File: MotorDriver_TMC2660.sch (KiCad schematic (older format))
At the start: 16 parts, among them U4 TMC2660

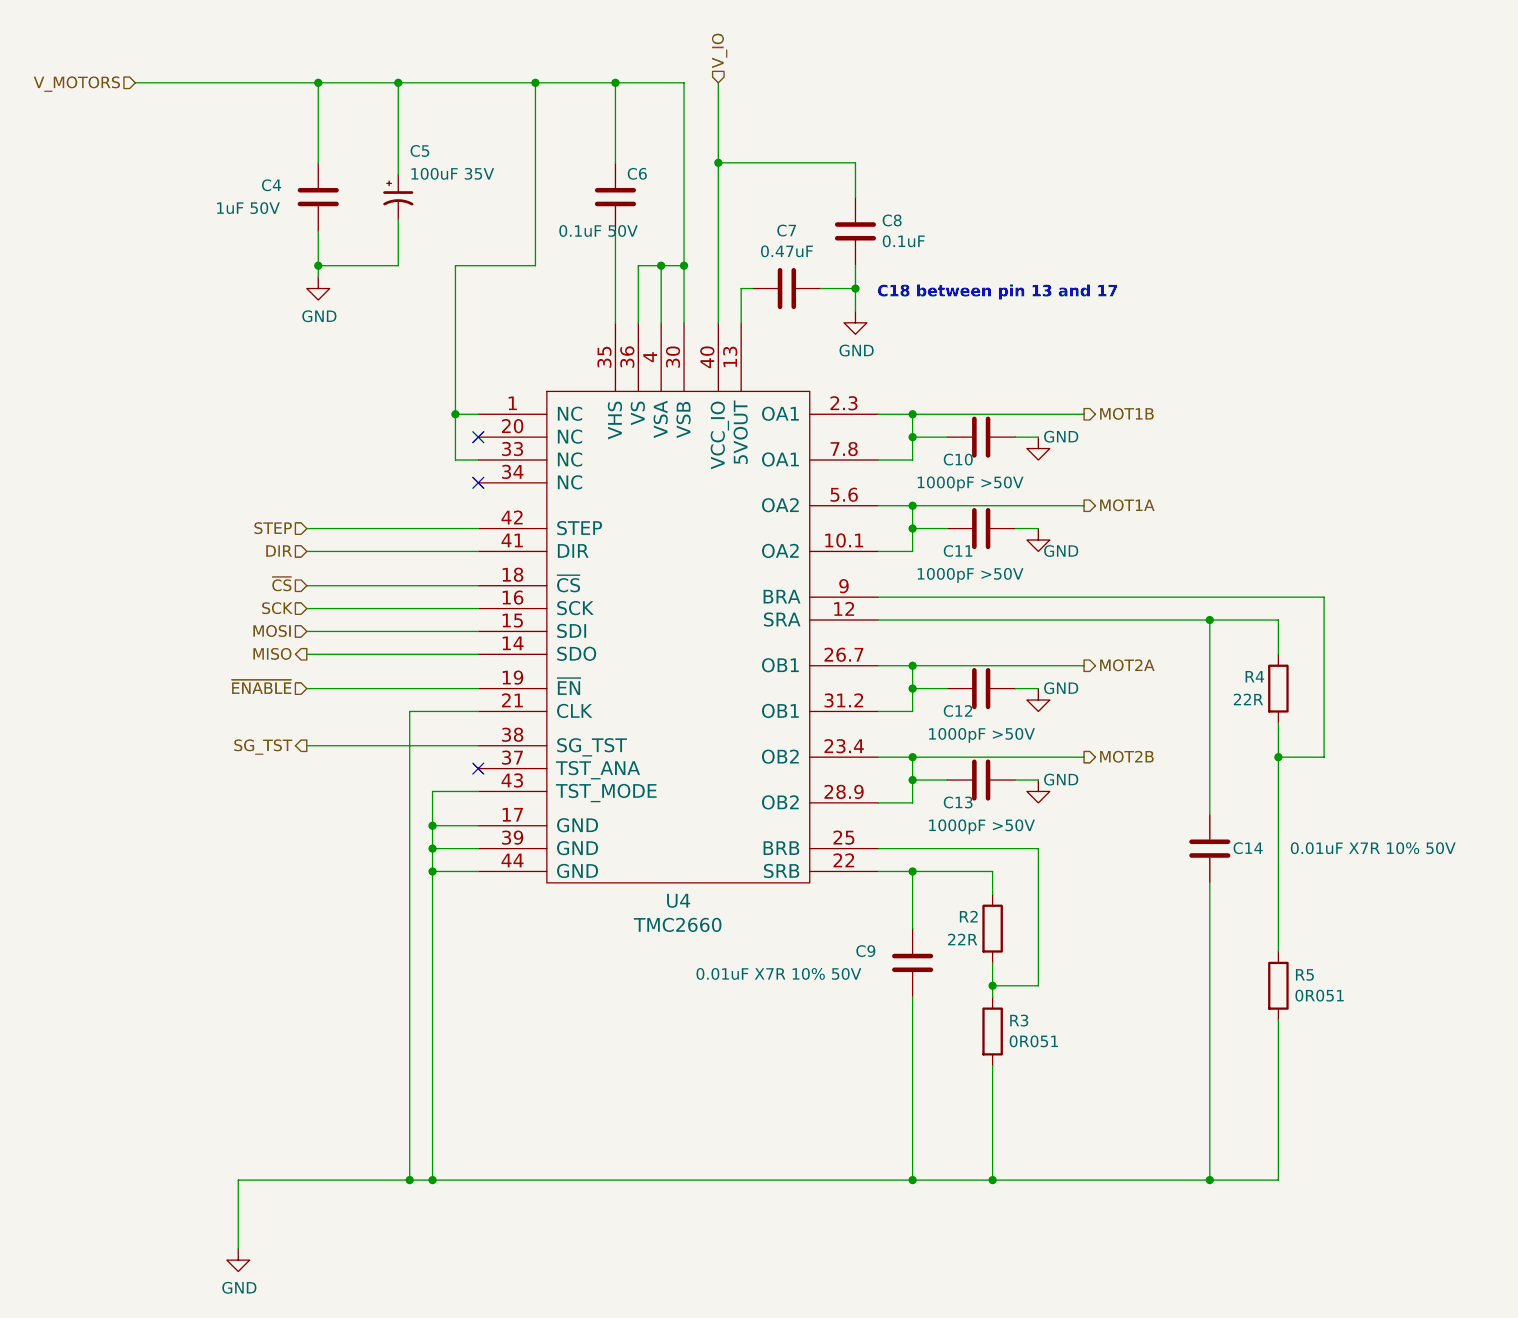
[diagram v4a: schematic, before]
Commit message: Assigned footprints for all components. Inductors are approximate size. MOSFETs dont agree with the footprints. Saved pcb netlist report as report.txt.
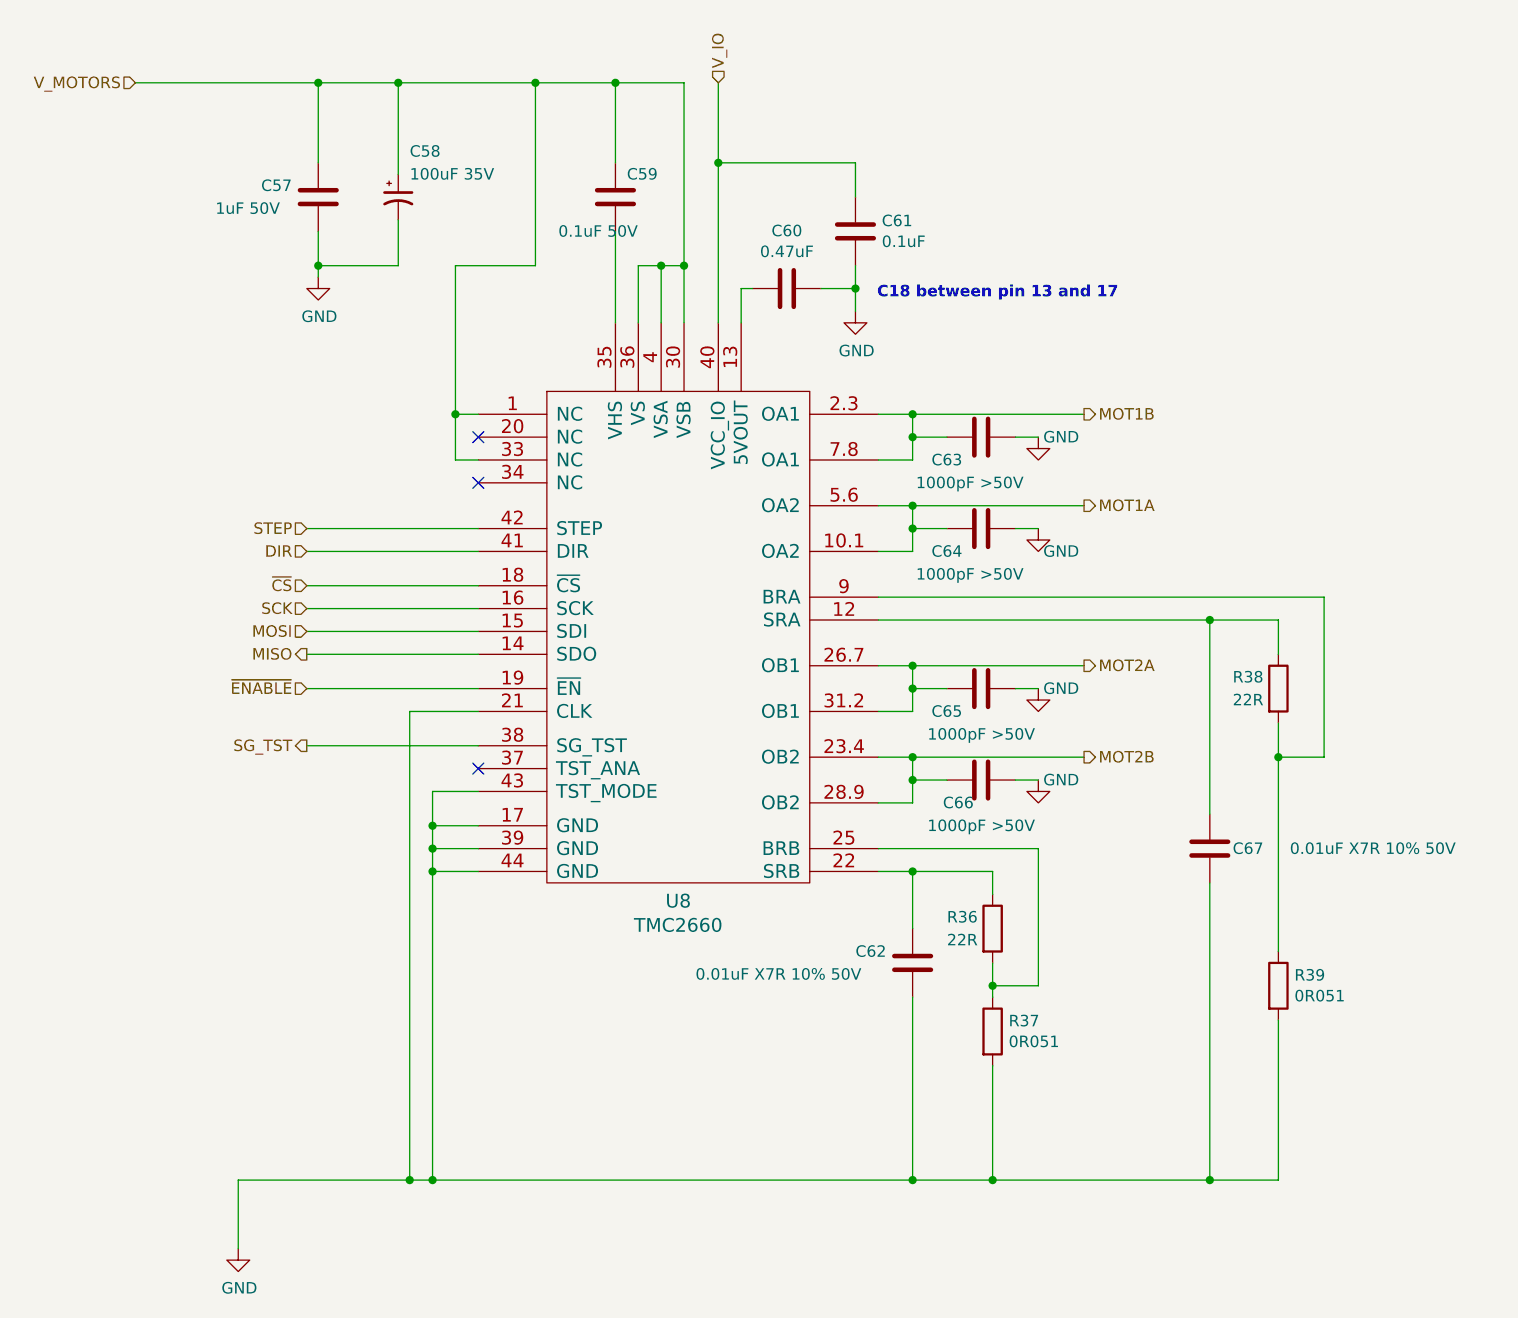
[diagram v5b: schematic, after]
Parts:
- C10, C11, C12, C13, C14, C4, C6, C7, C8, C9: footprint (none) -> Capacitor_SMD:C_0603_1608Metric
- C5: footprint (none) -> Capacitor_SMD:CP_Elec_6.3x7.7
- R2, R4: footprint (none) -> Resistor_SMD:R_0603_1608Metric
- R3, R5: footprint (none) -> Resistor_SMD:R_1206_3216Metric
- U4: footprint (none) -> PrntrBoardV1:TMC2660
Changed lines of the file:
@@
 $Descr A4 11693 8268
 encoding utf-8
-Sheet 9 35
+Sheet 26 35
 Title ""
 Date ""
@@
 AR Path="/5AC337B6/5ACE1C6D/5ACC0B66/5AC338BF" Ref="U7"  Part="1"
 AR Path="/5AC337B6/5AD9F95A/5AD4B0F5/5AC338BF" Ref="U8"  Part="1"
-F 0 "U4" H 4875 2520 60  0000 C CNN
+F 0 "U8" H 4875 2520 60  0000 C CNN
 F 1 "TMC2660" H 4875 2414 60  0000 C CNN
-F 2 "" H 4900 3600 60  0000 C CNN
+F 2 "PrntrBoardV1:TMC2660" H 4900 3600 60  0001 C CNN
 F 3 "" H 4900 3600 60  0000 C CNN
 	1    4900 3650
@@
 AR Path="/5AC337B6/5ACE1C6D/5ACC0B66/5AC33A94" Ref="C46"  Part="1"
 AR Path="/5AC337B6/5AD9F95A/5AD4B0F5/5AC33A94" Ref="C59"  Part="1"
-F 0 "C6" H 4650 1800 50  0000 L CNN
+F 0 "C59" H 4650 1800 50  0000 L CNN
 F 1 "0.1uF 50V" H 4350 1550 50  0000 L CNN
-F 2 "" H 4638 1550 50  0001 C CNN
+F 2 "Capacitor_SMD:C_0603_1608Metric" H 4638 1550 50  0001 C CNN
 F 3 "~" H 4600 1700 50  0001 C CNN
 	1    4600 1700
@@
 AR Path="/5AC337B6/5ACE1C6D/5ACC0B66/5AC33B3C" Ref="C44"  Part="1"
 AR Path="/5AC337B6/5AD9F95A/5AD4B0F5/5AC33B3C" Ref="C57"  Part="1"
-F 0 "C4" H 3050 1750 50  0000 L CNN
+F 0 "C57" H 3050 1750 50  0000 L CNN
 F 1 "1uF 50V" H 2850 1650 50  0000 L CNN
-F 2 "" H 3338 1550 50  0001 C CNN
+F 2 "Capacitor_SMD:C_0603_1608Metric" H 3338 1550 50  0001 C CNN
 F 3 "~" H 3300 1700 50  0001 C CNN
 	1    3300 1700
@@
 AR Path="/5AC337B6/5ACE1C6D/5ACC0B66/5AC33B85" Ref="C47"  Part="1"
 AR Path="/5AC337B6/5AD9F95A/5AD4B0F5/5AC33B85" Ref="C60"  Part="1"
-F 0 "C7" V 5098 2100 50  0000 C CNN
+F 0 "C60" V 5098 2100 50  0000 C CNN
 F 1 "0.47uF" V 5189 2100 50  0000 C CNN
-F 2 "" H 5388 1950 50  0001 C CNN
+F 2 "Capacitor_SMD:C_0603_1608Metric" H 5388 1950 50  0001 C CNN
 F 3 "~" H 5350 2100 50  0001 C CNN
 	1    5350 2100
@@
 AR Path="/5AC337B6/5ACE1C6D/5ACC0B66/5AC33C56" Ref="C48"  Part="1"
 AR Path="/5AC337B6/5AD9F95A/5AD4B0F5/5AC33C56" Ref="C61"  Part="1"
-F 0 "C8" H 5765 1896 50  0000 L CNN
+F 0 "C61" H 5765 1896 50  0000 L CNN
 F 1 "0.1uF" H 5765 1805 50  0000 L CNN
-F 2 "" H 5688 1700 50  0001 C CNN
+F 2 "Capacitor_SMD:C_0603_1608Metric" H 5688 1700 50  0001 C CNN
 F 3 "~" H 5650 1850 50  0001 C CNN
 	1    5650 1850
@@
 AR Path="/5AC337B6/5ACE1C6D/5ACC0B66/5AC33CA1" Ref="C50"  Part="1"
 AR Path="/5AC337B6/5AD9F95A/5AD4B0F5/5AC33CA1" Ref="C63"  Part="1"
-F 0 "C10" V 6300 2650 50  0000 C CNN
+F 0 "C63" V 6300 2600 50  0000 C CNN
 F 1 "1000pF >50V" V 6400 2700 50  0000 C CNN
-F 2 "" H 6238 2600 50  0001 C CNN
+F 2 "Capacitor_SMD:C_0603_1608Metric" H 6238 2600 50  0001 C CNN
 F 3 "~" H 6200 2750 50  0001 C CNN
 	1    6200 2750
@@
 AR Path="/5AC337B6/5ACE1C6D/5ACC0B66/5AC33D6E" Ref="C51"  Part="1"
 AR Path="/5AC337B6/5AD9F95A/5AD4B0F5/5AC33D6E" Ref="C64"  Part="1"
-F 0 "C11" V 6300 3050 50  0000 C CNN
+F 0 "C64" V 6300 3000 50  0000 C CNN
 F 1 "1000pF >50V" V 6400 3100 50  0000 C CNN
-F 2 "" H 6238 3000 50  0001 C CNN
+F 2 "Capacitor_SMD:C_0603_1608Metric" H 6238 3000 50  0001 C CNN
 F 3 "~" H 6200 3150 50  0001 C CNN
 	1    6200 3150
@@
 AR Path="/5AC337B6/5ACE1C6D/5ACC0B66/5AC33DC1" Ref="C52"  Part="1"
 AR Path="/5AC337B6/5AD9F95A/5AD4B0F5/5AC33DC1" Ref="C65"  Part="1"
-F 0 "C12" V 6300 3750 50  0000 C CNN
+F 0 "C65" V 6300 3700 50  0000 C CNN
 F 1 "1000pF >50V" V 6400 3850 50  0000 C CNN
-F 2 "" H 6238 3700 50  0001 C CNN
+F 2 "Capacitor_SMD:C_0603_1608Metric" H 6238 3700 50  0001 C CNN
 F 3 "~" H 6200 3850 50  0001 C CNN
 	1    6200 3850
@@
 AR Path="/5AC337B6/5ACE1C6D/5ACC0B66/5AC33E6E" Ref="C53"  Part="1"
 AR Path="/5AC337B6/5AD9F95A/5AD4B0F5/5AC33E6E" Ref="C66"  Part="1"
-F 0 "C13" V 6300 4150 50  0000 C CNN
+F 0 "C66" V 6300 4150 50  0000 C CNN
 F 1 "1000pF >50V" V 6400 4250 50  0000 C CNN
-F 2 "" H 6238 4100 50  0001 C CNN
+F 2 "Capacitor_SMD:C_0603_1608Metric" H 6238 4100 50  0001 C CNN
 F 3 "~" H 6200 4250 50  0001 C CNN
 	1    6200 4250
@@
 AR Path="/5AC337B6/5ACE1C6D/5ACC0B66/5AC33EDF" Ref="C54"  Part="1"
 AR Path="/5AC337B6/5AD9F95A/5AD4B0F5/5AC33EDF" Ref="C67"  Part="1"
-F 0 "C14" H 7300 4550 50  0000 L CNN
+F 0 "C67" H 7300 4550 50  0000 L CNN
 F 1 "0.01uF X7R 10% 50V" H 7550 4550 50  0000 L CNN
-F 2 "" H 7238 4400 50  0001 C CNN
+F 2 "Capacitor_SMD:C_0603_1608Metric" H 7238 4400 50  0001 C CNN
 F 3 "~" H 7200 4550 50  0001 C CNN
 	1    7200 4550
@@
 AR Path="/5AC337B6/5ACE1C6D/5ACC0B66/5AC33F7D" Ref="C49"  Part="1"
 AR Path="/5AC337B6/5AD9F95A/5AD4B0F5/5AC33F7D" Ref="C62"  Part="1"
-F 0 "C9" H 5650 5100 50  0000 L CNN
+F 0 "C62" H 5650 5100 50  0000 L CNN
 F 1 "0.01uF X7R 10% 50V" H 4950 5000 50  0000 L CNN
-F 2 "" H 5938 4900 50  0001 C CNN
+F 2 "Capacitor_SMD:C_0603_1608Metric" H 5938 4900 50  0001 C CNN
 F 3 "~" H 5900 5050 50  0001 C CNN
 	1    5900 5050
@@
 AR Path="/5AC337B6/5ACE1C6D/5ACC0B66/5AC3912E" Ref="R28"  Part="1"
 AR Path="/5AC337B6/5AD9F95A/5AD4B0F5/5AC3912E" Ref="R36"  Part="1"
-F 0 "R2" H 6100 4950 50  0000 L CNN
+F 0 "R36" H 6050 4950 50  0000 L CNN
 F 1 "22R" H 6050 4850 50  0000 L CNN
-F 2 "" V 6180 4900 50  0001 C CNN
+F 2 "Resistor_SMD:R_0603_1608Metric" V 6180 4900 50  0001 C CNN
 F 3 "~" H 6250 4900 50  0001 C CNN
 	1    6250 4900
@@
 AR Path="/5AC337B6/5ACE1C6D/5ACC0B66/5AC391BE" Ref="R29"  Part="1"
 AR Path="/5AC337B6/5AD9F95A/5AD4B0F5/5AC391BE" Ref="R37"  Part="1"
-F 0 "R3" H 6320 5396 50  0000 L CNN
+F 0 "R37" H 6320 5396 50  0000 L CNN
 F 1 "0R051" H 6320 5305 50  0000 L CNN
-F 2 "" V 6180 5350 50  0001 C CNN
+F 2 "Resistor_SMD:R_1206_3216Metric" V 6180 5350 50  0001 C CNN
 F 3 "~" H 6250 5350 50  0001 C CNN
 	1    6250 5350
@@
 AR Path="/5AC337B6/5ACE1C6D/5ACC0B66/5AC3921D" Ref="R30"  Part="1"
 AR Path="/5AC337B6/5AD9F95A/5AD4B0F5/5AC3921D" Ref="R38"  Part="1"
-F 0 "R4" H 7350 3900 50  0000 L CNN
+F 0 "R38" H 7300 3900 50  0000 L CNN
 F 1 "22R" H 7300 3800 50  0000 L CNN
-F 2 "" V 7430 3850 50  0001 C CNN
+F 2 "Resistor_SMD:R_0603_1608Metric" V 7430 3850 50  0001 C CNN
 F 3 "~" H 7500 3850 50  0001 C CNN
 	1    7500 3850
@@
 AR Path="/5AC337B6/5ACE1C6D/5ACC0B66/5AC392A1" Ref="R31"  Part="1"
 AR Path="/5AC337B6/5AD9F95A/5AD4B0F5/5AC392A1" Ref="R39"  Part="1"
-F 0 "R5" H 7570 5196 50  0000 L CNN
+F 0 "R39" H 7570 5196 50  0000 L CNN
 F 1 "0R051" H 7570 5105 50  0000 L CNN
-F 2 "" V 7430 5150 50  0001 C CNN
+F 2 "Resistor_SMD:R_1206_3216Metric" V 7430 5150 50  0001 C CNN
 F 3 "~" H 7500 5150 50  0001 C CNN
 	1    7500 5150
@@
 AR Path="/5AC337B6/5ACE1C6D/5ACC0B66/5AC55FA7" Ref="C45"  Part="1"
 AR Path="/5AC337B6/5AD9F95A/5AD4B0F5/5AC55FA7" Ref="C58"  Part="1"
-F 0 "C5" H 3700 1900 50  0000 L CNN
+F 0 "C58" H 3700 1900 50  0000 L CNN
 F 1 "100uF 35V" H 3700 1800 50  0000 L CNN
-F 2 "" H 3650 1700 50  0001 C CNN
+F 2 "Capacitor_SMD:CP_Elec_6.3x7.7" H 3650 1700 50  0001 C CNN
 F 3 "~" H 3650 1700 50  0001 C CNN
 	1    3650 1700
